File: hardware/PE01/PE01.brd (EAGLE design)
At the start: 25.4 x 27 mm, 23 parts, among them IC1 MSP430G2231, IC2 LP2982M5

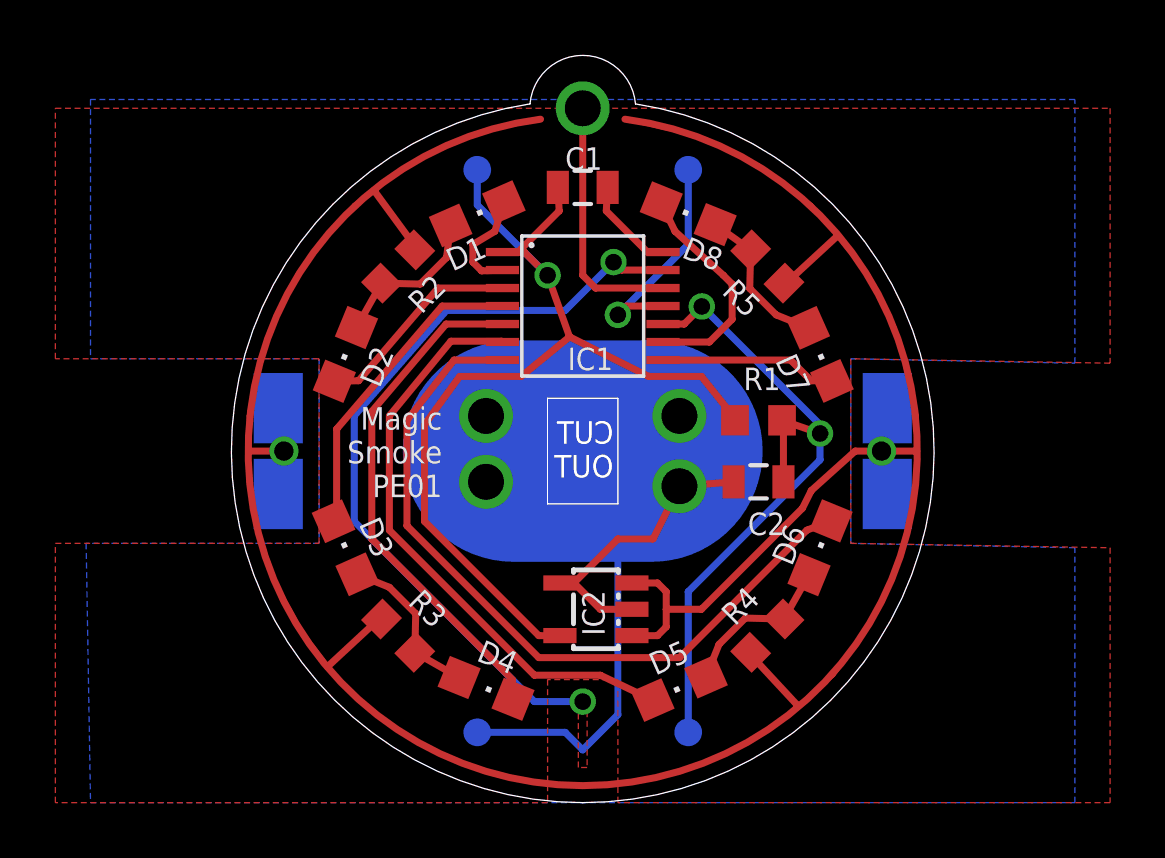
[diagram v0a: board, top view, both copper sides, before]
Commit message: Fixed GND, removed slot
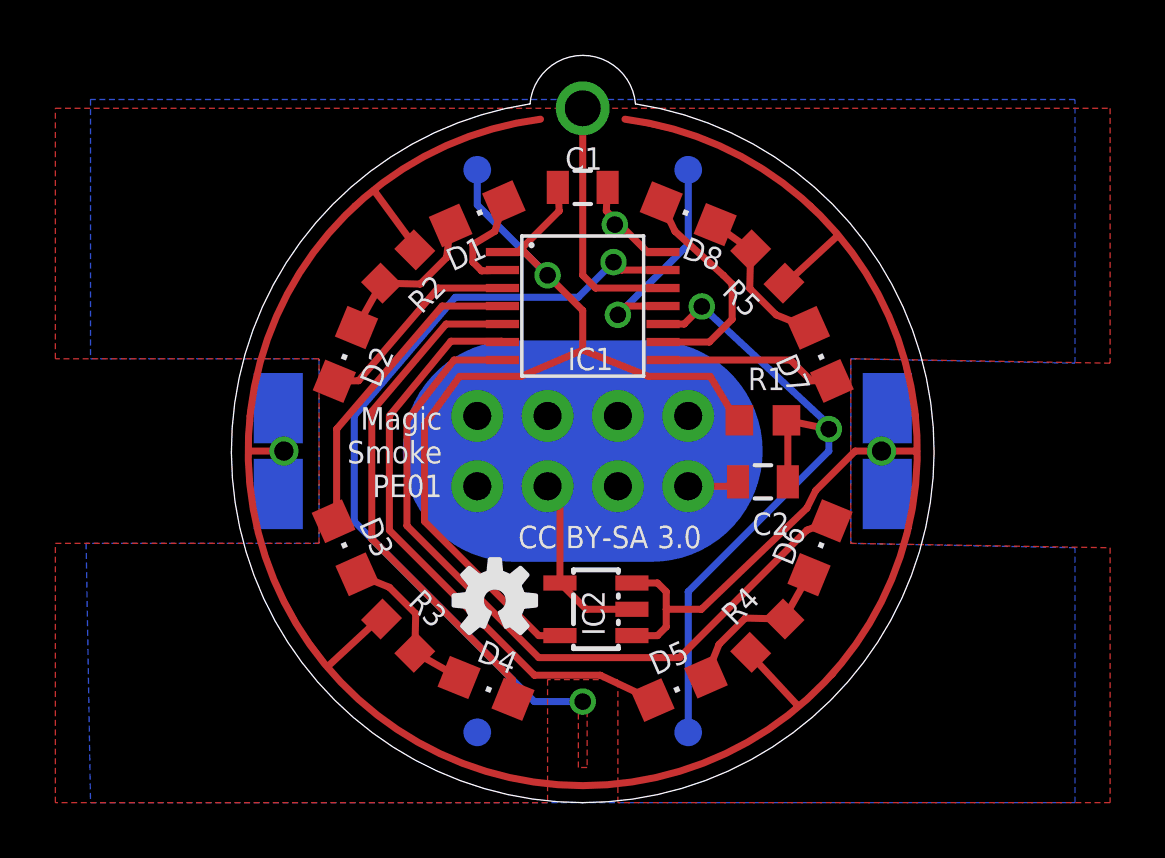
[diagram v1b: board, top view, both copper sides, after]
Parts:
- added JP1, JP2, JP3, JP4: (no value), SparkFun:1X02_NO_SILK
- IC2: value LP2982M5 -> TPS78233
- moved U$1 14.0 mm to (47.6, 50.5), flipped to the top
- moved C2 0.16 mm to (57.3, 54.8)
- moved R1 0.16 mm to (57.3, 57.0)
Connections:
- removed net N$13: C1.2, IC1.14
- net GND: now also C1.2, IC1.14, JP1.1, JP1.2, JP2.1, JP2.2, JP3.1, JP3.2, JP4.1, JP4.2
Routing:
- net GND: track 40.8 -> 31.6 mm, vias 4 -> 1
- net N$13: track 3.52 -> 0.00 mm
- net +3V3: track 36.6 -> 37.2 mm
- added copper zone on layer 1, net GND
- removed copper zone on layer 1, net N$14
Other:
- outline, holes or cut-outs redrawn
- board text added: "CC BY-SA 3.0"
- board text removed: "CUT OUT"
